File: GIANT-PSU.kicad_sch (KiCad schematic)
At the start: 71 parts, among them Q1 2SA562, Q2 2SC1684, Q3 2SC1815, Q9 2SC3376, SW1 Power Switch, T1 APII_EI35, U1 4N37, U2 LM7805_TO220, U3 LM7812_TO220, U4 uA431A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

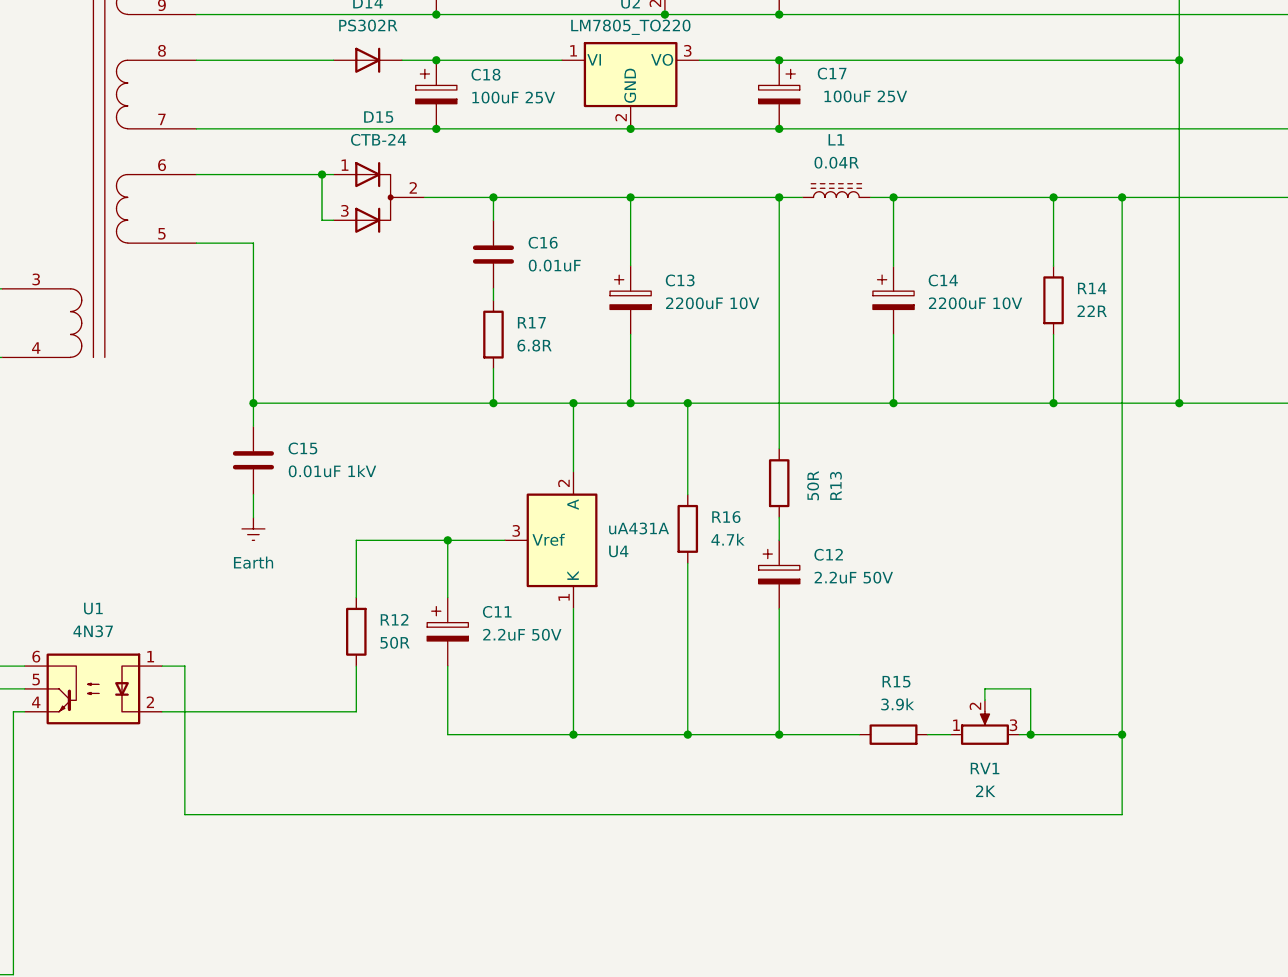
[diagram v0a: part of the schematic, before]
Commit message: Minor correction to shunt voltage regulator schematic.
Signed-off-by: Khralkatorrix <garuda2550@gmail.com>
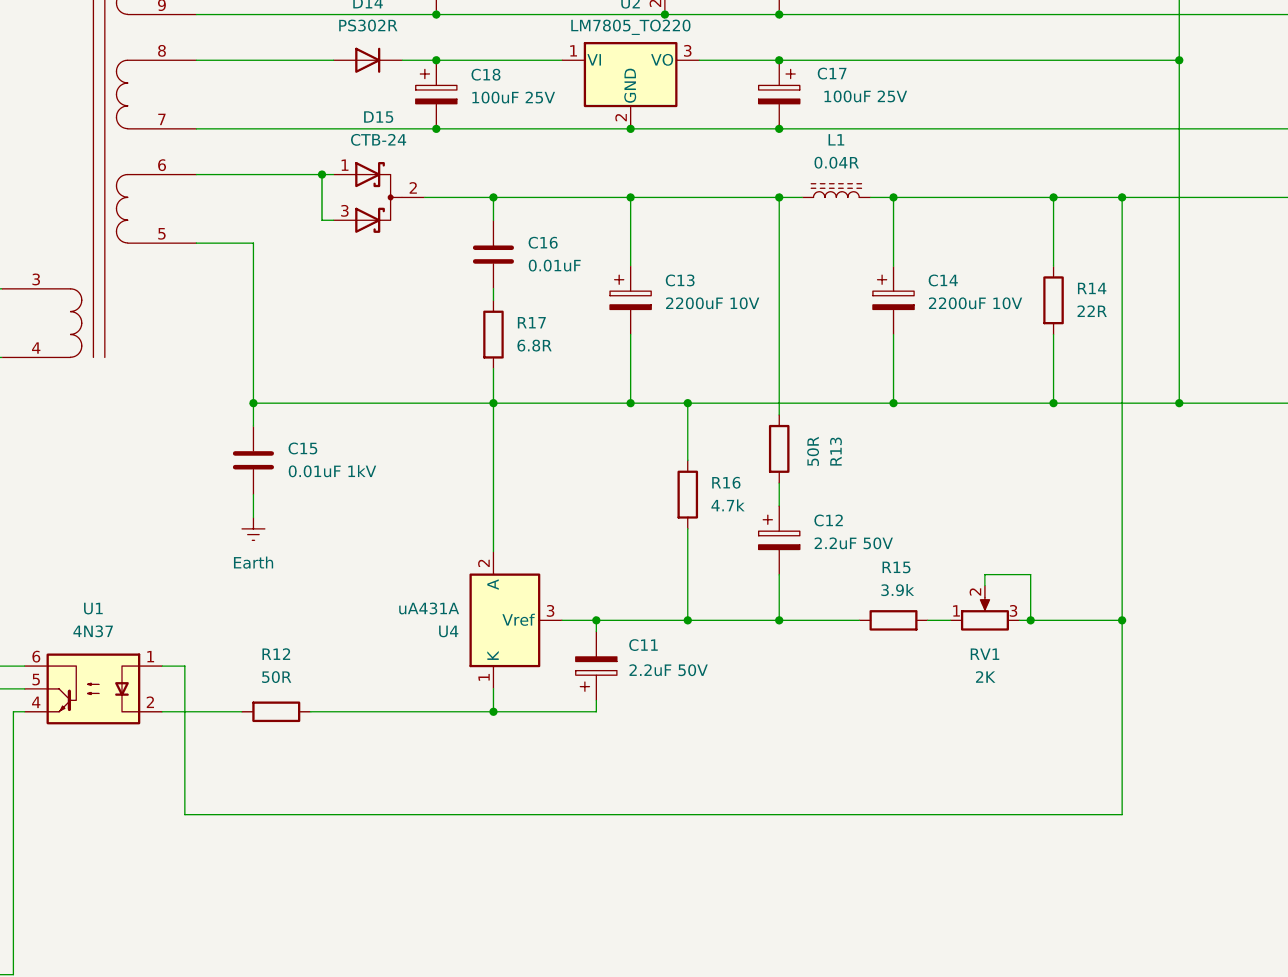
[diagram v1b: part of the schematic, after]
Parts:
- removed D15: CTB-24, symbol Device:D_Dual_CommonCathode_AKA_Parallel
- added D15: CTB-24, symbol Device:D_Schottky_Dual_CommonCathode_AKA_Parallel
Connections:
- net at C11.2, C12.2, R15.1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: now also U4.3 (Vref); no longer U4.1 (K)
- net at C13.1, C16.1, L1.1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: now also D15.2 (K)
- net at R12.1: now also C11.1, U4.1 (K); no longer U1.2
- net at T1.6 (SD): now also D15.1 (A), D15.3 (A)
- new net: R12.2, U1.2
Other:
- moved on the sheet: C11, C12, R12, R13, R15, R16, RV1, U4
